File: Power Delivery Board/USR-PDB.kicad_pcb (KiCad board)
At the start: 2 copper layers, 86.1 x 166.1 mm, 45 parts, among them IC1 LM7805ECT, IC2 LM7805ECT, J1 XT90PW-M, U10 Anderson PP45 Vert. 2x1, U11 Anderson PP45 Vert. 2x1, U12 Anderson PP45 Vert. 2x1, U14 MCP3002-I/P, U17 AMS1117-3.3, U2 Anderson PP45 Vert. 2x1, U3 Anderson PP45 Vert. 2x1, U4 Anderson PP45 Vert. 2x1, U5 Anderson PP45 Vert. 2x1, U6 Anderson PP45 Vert. 2x1, U7 LM2676T-12_NOPB

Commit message: Final PDB tweaks. New production run.
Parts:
- added U1: ~, USR:JST-XA 3-PIN, F.Cu at (50.6, 23.1)
- added U13: ~, USR:JST-XA 3-PIN, F.Cu at (63.3, 23.1)
- F3, F4, F5: value Fuse Holder: 5A -> Fuse Holder: 30A
- F6: value Fuse Holder: 7A -> Fuse Holder: 30A
- F7: value Extra fuse holder -> Fuse Holder: 30A
- F8: value Fuse Holder: 3A -> Fuse Holder: 30A
- G***: moved to B.Cu
- moved D1 14.0 mm to (78.7, 171.4), turned to -90 degrees
- moved J1 9.87 mm to (87.3, 24.1)
- moved C4 5.26 mm to (88.9, 181.5)
- moved G*** 2.84 mm to (101.6, 41.9), turned to 180 degrees
- moved C3 2.54 mm to (99.1, 181.3)
- moved U15 0.08 mm to (37.5, 38.1)
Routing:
- net HE1_out: track 11.4 -> 26.2 mm
- net Net-(D1-K): track 35.7 -> 22.3 mm
- net HE2_out: track 41.3 -> 51.3 mm
- net Net-(U7-VIN): track 39.1 -> 45.9 mm
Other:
- board text added: "ADC to Pico (SPI)"
- board text added: "HE1"
- board text added: "HE2"
- board text removed: "ADC to pico comms"

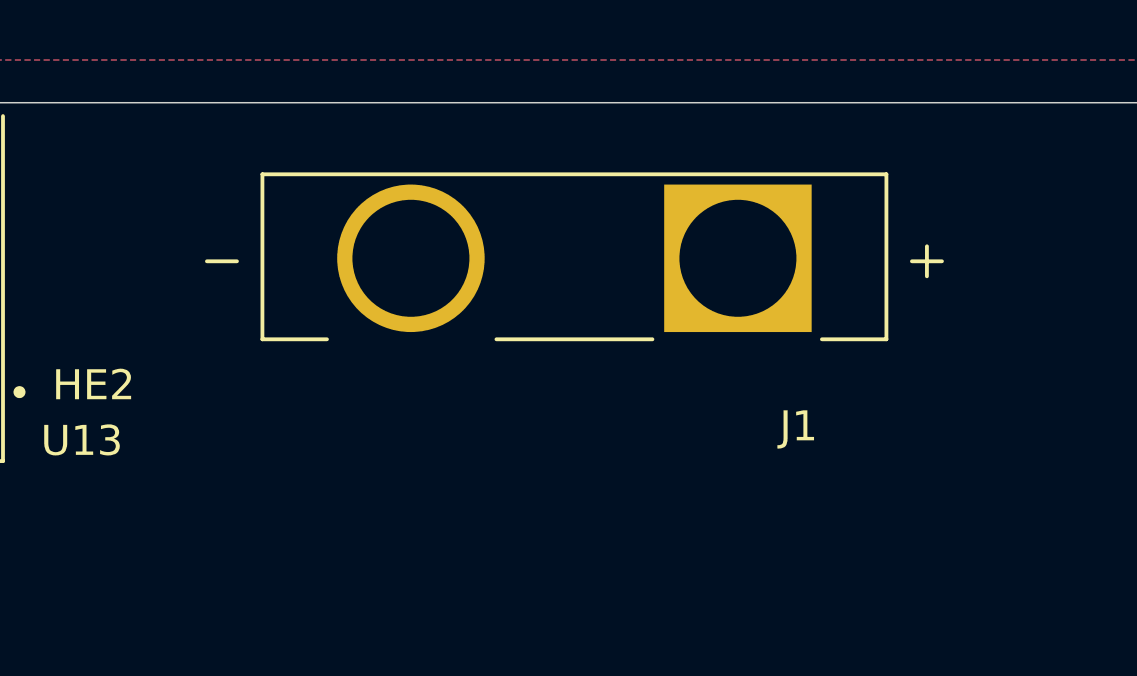
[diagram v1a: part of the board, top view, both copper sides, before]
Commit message: Updated PCB designs across the motor driver, analog board, and PDB
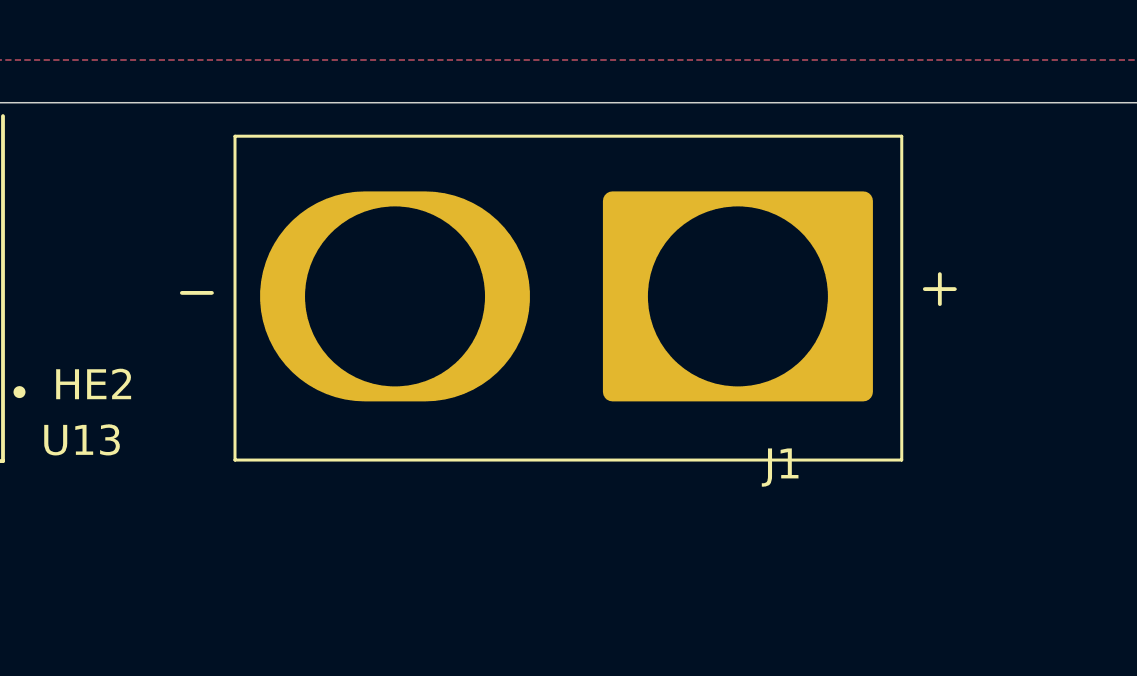
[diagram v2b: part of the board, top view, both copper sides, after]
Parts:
- moved G*** 4.58 mm to (105.4, 44.5)
- moved J1 1.37 mm to (86.7, 25.4)
